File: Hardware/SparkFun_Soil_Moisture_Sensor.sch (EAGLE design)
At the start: 10 parts, among them Q1 2N3904

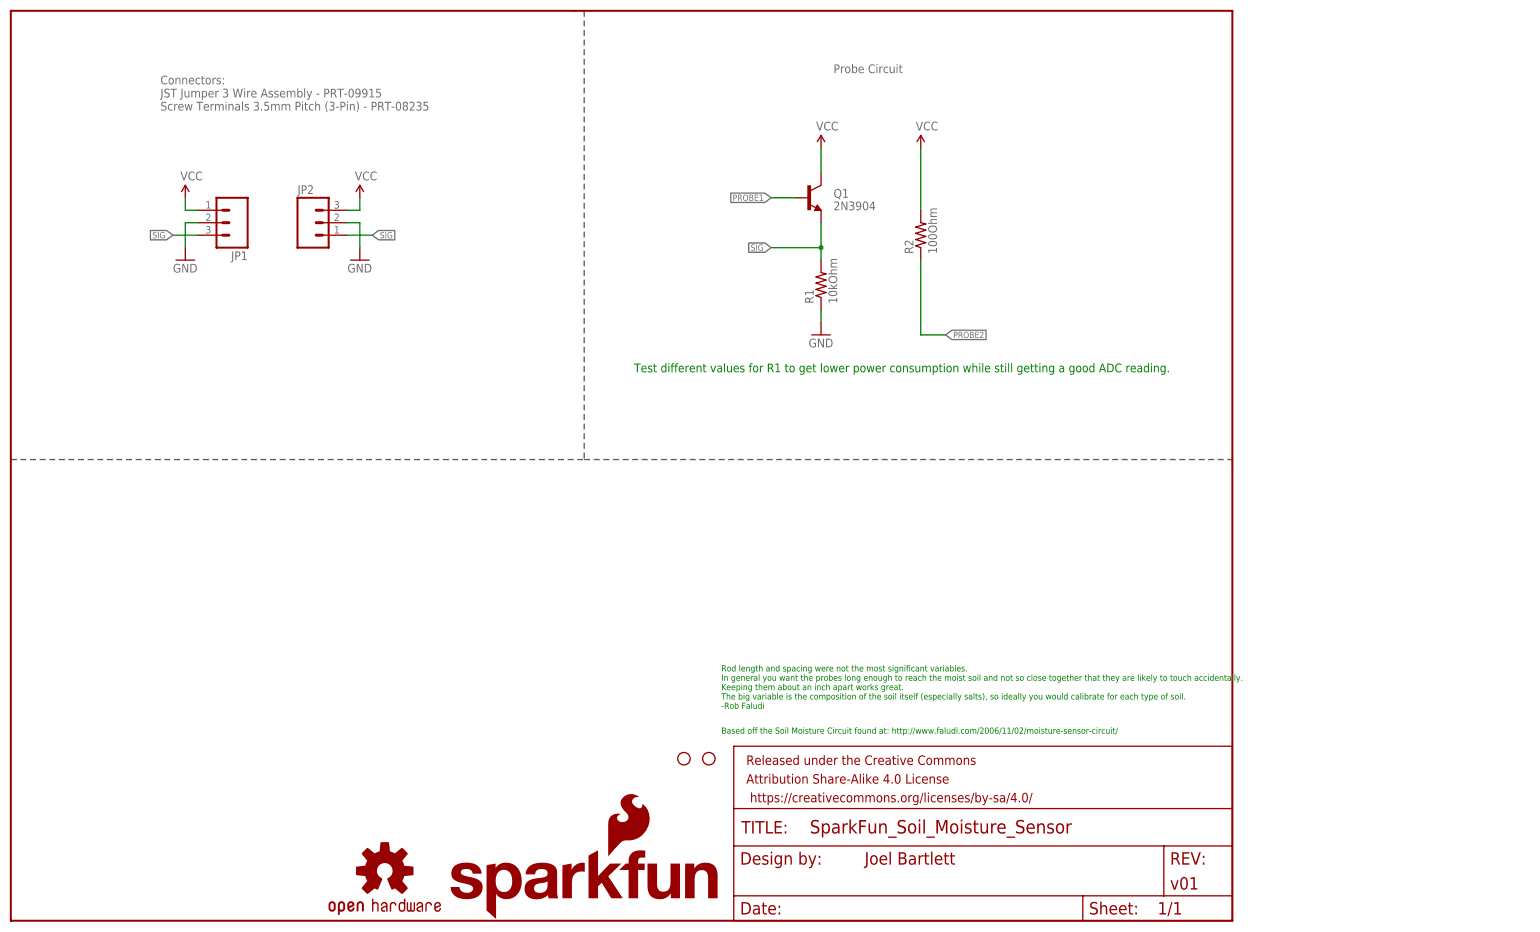
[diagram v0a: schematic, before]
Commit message: Fixed QC Checklist issues
added fiducials, changed dimension width to .008, removed Ohm from
values, added Vcc range, changed version # to correct V01, corrected
dashed lines
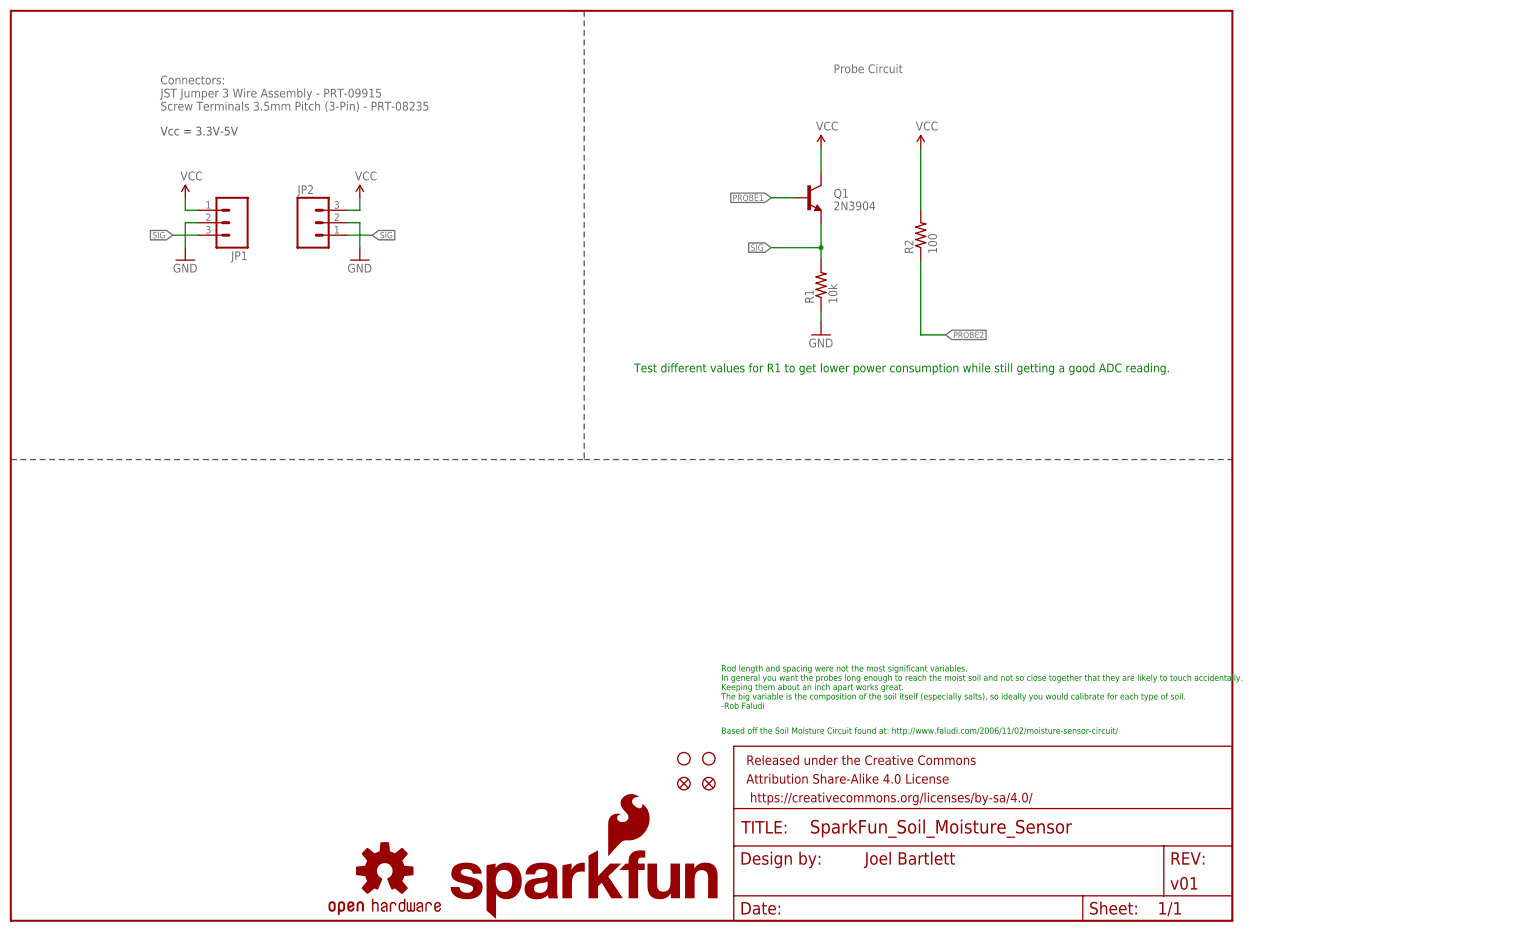
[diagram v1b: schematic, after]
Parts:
- added FID1, FID2: FIDUCIAL1X2, SparkFun-Aesthetics:FIDUCIAL1X2
- R1: value 10kOhm -> 10k
- R2: value 100Ohm -> 100
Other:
- note added: "Vcc = 3.3V-5V"
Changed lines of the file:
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@@
 <parts>
 <part name="Q1" library="SparkFun-DiscreteSemi" deviceset="TRANSISTOR_NPN" device="MMBT2222A" value="2N3904"/>
-<part name="R1" library="SparkFun-Resistors" deviceset="100OHM-1/4W-5%(0603)" device="" value="10kOhm"/>
+<part name="R1" library="SparkFun-Resistors" deviceset="100OHM-1/4W-5%(0603)" device="" value="10k"/>
 <part name="SUPPLY1" library="SparkFun-Aesthetics" deviceset="VCC" device=""/>
 <part name="GND1" library="SparkFun-Aesthetics" deviceset="GND" device=""/>
-<part name="R2" library="SparkFun-Resistors" deviceset="100OHM-1/4W-5%(0603)" device="" value="100Ohm"/>
+<part name="R2" library="SparkFun-Resistors" deviceset="100OHM-1/4W-5%(0603)" device="" value="100"/>
 <part name="SUPPLY2" library="SparkFun-Aesthetics" deviceset="VCC" device=""/>
 <part name="SUPPLY3" library="SparkFun-Aesthetics" deviceset="VCC" device=""/>
@@
 <part name="STANDOFF1" library="SparkFun-Electromechanical" deviceset="STAND-OFF" device=""/>
 <part name="STANDOFF2" library="SparkFun-Electromechanical" deviceset="STAND-OFF" device=""/>
+<part name="FID1" library="SparkFun-Aesthetics" deviceset="FIDUCIAL" device="1X2"/>
+<part name="FID2" library="SparkFun-Aesthetics" deviceset="FIDUCIAL" device="1X2"/>
 </parts>
 <sheets>
@@
 <plain>
 <text x="127" y="111.76" size="1.778" layer="91">Test different values for R1 to get lower power consumption while still getting a good ADC reading. </text>
-<wire x1="0" y1="93.98" x2="116.84" y2="93.98" width="0.2032" layer="97" style="dashdot"/>
-<wire x1="116.84" y1="93.98" x2="248.92" y2="93.98" width="0.2032" layer="97" style="dashdot"/>
+<wire x1="0" y1="93.98" x2="116.84" y2="93.98" width="0.2032" layer="97" style="shortdash"/>
+<wire x1="116.84" y1="93.98" x2="248.92" y2="93.98" width="0.2032" layer="97" style="shortdash"/>
 <wire x1="248.92" y1="93.98" x2="248.92" y2="91.44" width="0.2032" layer="97" style="dashdot"/>
 <wire x1="114.3" y1="185.42" x2="116.84" y2="185.42" width="0.2032" layer="97" style="dashdot"/>
-<wire x1="116.84" y1="185.42" x2="116.84" y2="93.98" width="0.2032" layer="97" style="dashdot"/>
+<wire x1="116.84" y1="185.42" x2="116.84" y2="93.98" width="0.2032" layer="97" style="shortdash"/>
 <text x="144.78" y="38.1" size="1.27" layer="91">Based off the Soil Moisture Circuit found at: http://www.faludi.com/2006/11/02/moisture-sensor-circuit/</text>
 <text x="144.78" y="43.18" size="1.27" layer="91">Rod length and spacing were not the most significant variables.
@@
 Screw Terminals 3.5mm Pitch (3-Pin) - PRT-08235</text>
 <text x="167.64" y="172.72" size="1.778" layer="95">Probe Circuit</text>
+<text x="30.48" y="160.02" size="1.778" layer="97">Vcc = 3.3V-5V</text>
 </plain>
 <instances>
@@
 <instance part="STANDOFF1" gate="G$1" x="137.16" y="33.02"/>
 <instance part="STANDOFF2" gate="G$1" x="142.24" y="33.02"/>
+<instance part="FID1" gate="G$1" x="137.16" y="27.94"/>
+<instance part="FID2" gate="G$1" x="142.24" y="27.94"/>
 </instances>
 <busses>

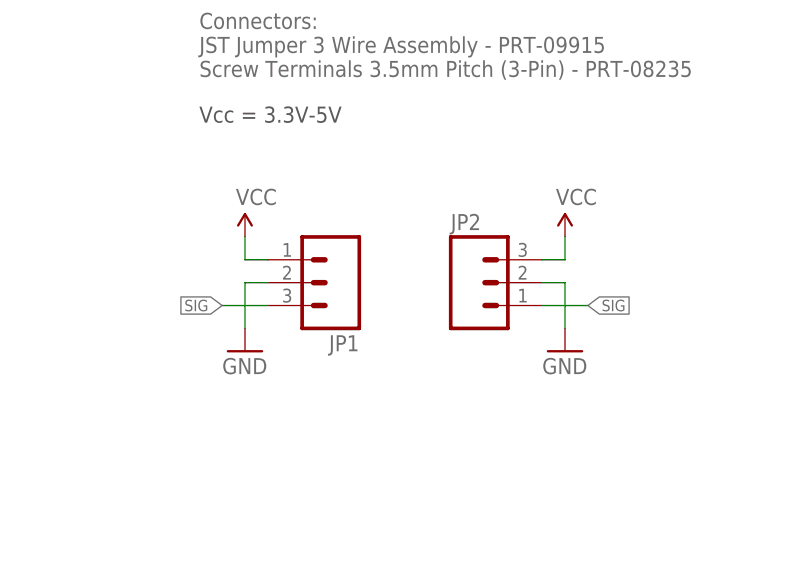
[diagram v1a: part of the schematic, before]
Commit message: Ready for QC checklist
thickened traces, few minor aesthetic changes. Updated version #.
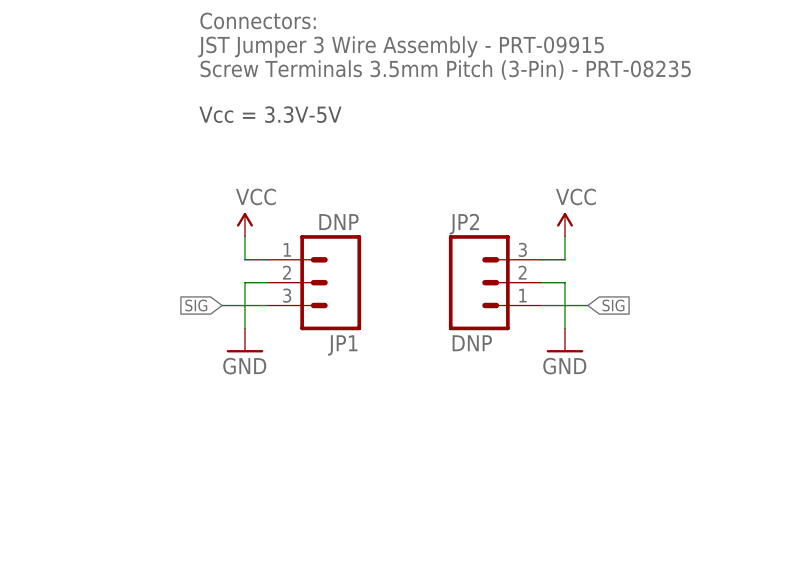
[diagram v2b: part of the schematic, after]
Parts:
- JP1, JP2: value (none) -> DNP
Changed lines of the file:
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@@
 <part name="LOGO1" library="SparkFun-Aesthetics" deviceset="SFE_LOGO_NAME_FLAME" device=".1_INCH"/>
 <part name="LOGO2" library="SparkFun-Aesthetics" deviceset="OSHW-LOGO" device="S"/>
-<part name="JP1" library="SparkFun-Connectors" deviceset="M03" device="POLAR"/>
-<part name="JP2" library="SparkFun-Connectors" deviceset="M03" device="SCREW"/>
+<part name="JP1" library="SparkFun-Connectors" deviceset="M03" device="POLAR" value="DNP"/>
+<part name="JP2" library="SparkFun-Connectors" deviceset="M03" device="SCREW" value="DNP"/>
 <part name="SUPPLY4" library="SparkFun-Aesthetics" deviceset="VCC" device=""/>
 <part name="GND3" library="SparkFun-Aesthetics" deviceset="GND" device=""/>

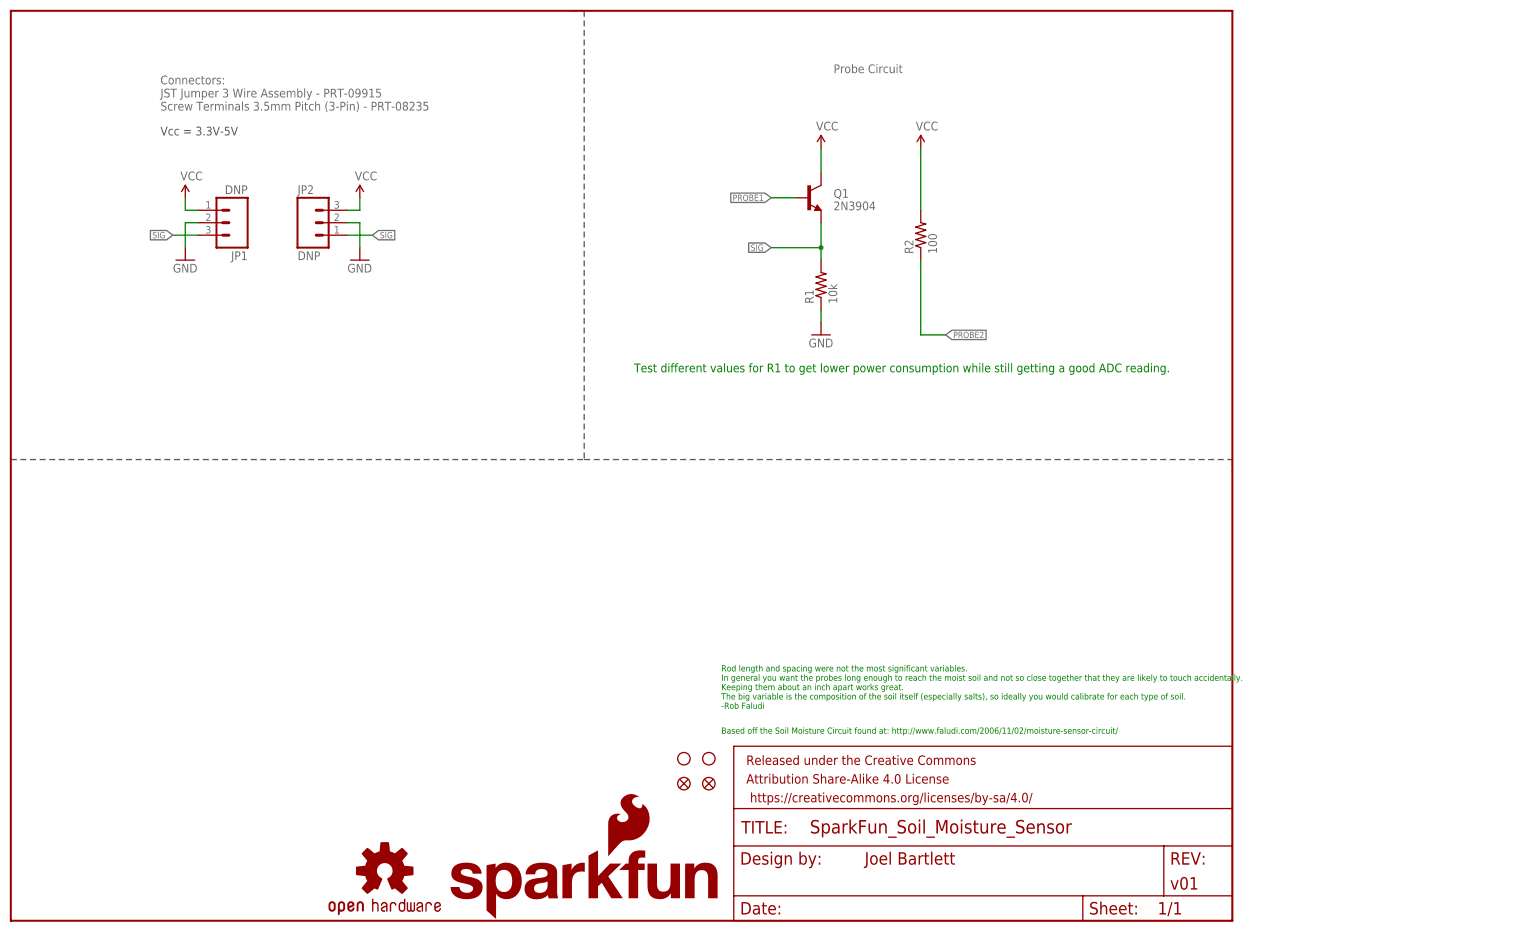
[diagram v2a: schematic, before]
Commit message: Ready for Reds
Passed QC check #2
-Comments to layer 97
-Updated Version # on SCH.
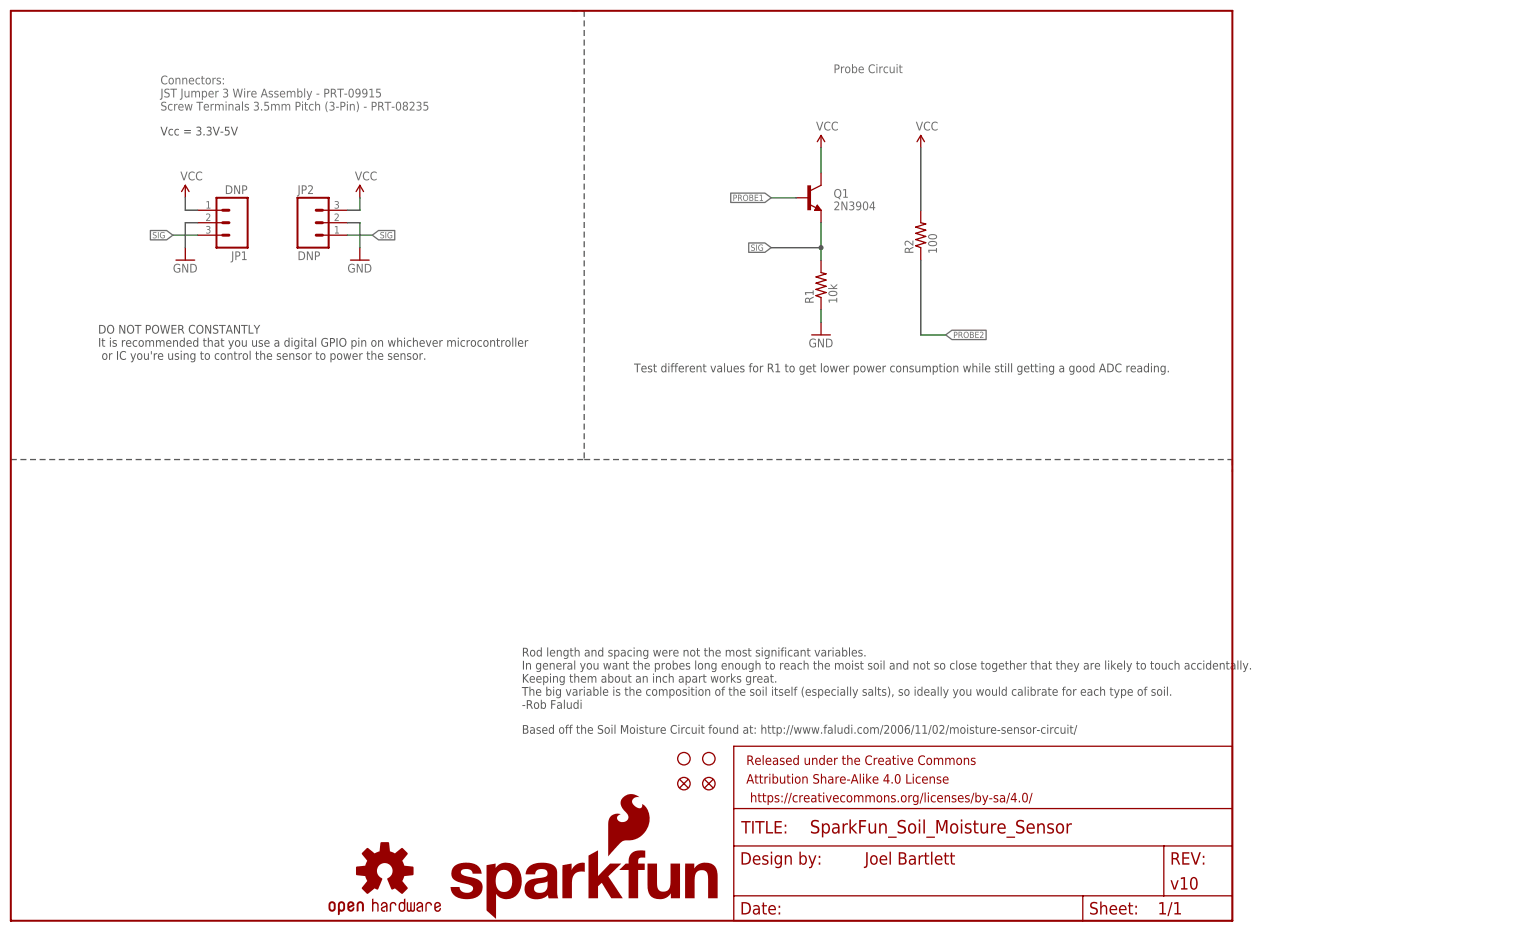
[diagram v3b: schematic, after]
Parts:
- FRAME1: VERSION (none) -> v10
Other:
- note added: "DO NOT POWER CONSTANTLY It is recommended that you use a digital GPIO pin on whichever microcontroller or IC you're using to control the sensor to power the sensor."
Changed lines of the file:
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@@
 <part name="FRAME1" library="SparkFun-Aesthetics" deviceset="FRAME-LETTER" device="">
 <attribute name="DESIGNER" value="Joel Bartlett"/>
+<attribute name="VERSION" value="v10"/>
 </part>
 <part name="LOGO1" library="SparkFun-Aesthetics" deviceset="SFE_LOGO_NAME_FLAME" device=".1_INCH"/>
@@
 <sheet>
 <plain>
-<text x="127" y="111.76" size="1.778" layer="91">Test different values for R1 to get lower power consumption while still getting a good ADC reading. </text>
+<text x="127" y="111.76" size="1.778" layer="97">Test different values for R1 to get lower power consumption while still getting a good ADC reading. </text>
 <wire x1="0" y1="93.98" x2="116.84" y2="93.98" width="0.2032" layer="97" style="shortdash"/>
 <wire x1="116.84" y1="93.98" x2="248.92" y2="93.98" width="0.2032" layer="97" style="shortdash"/>
@@
 <wire x1="114.3" y1="185.42" x2="116.84" y2="185.42" width="0.2032" layer="97" style="dashdot"/>
 <wire x1="116.84" y1="185.42" x2="116.84" y2="93.98" width="0.2032" layer="97" style="shortdash"/>
-<text x="144.78" y="38.1" size="1.27" layer="91">Based off the Soil Moisture Circuit found at: http://www.faludi.com/2006/11/02/moisture-sensor-circuit/</text>
-<text x="144.78" y="43.18" size="1.27" layer="91">Rod length and spacing were not the most significant variables.
+<text x="104.14" y="38.1" size="1.778" layer="97">Based off the Soil Moisture Circuit found at: http://www.faludi.com/2006/11/02/moisture-sensor-circuit/</text>
+<text x="104.14" y="43.18" size="1.778" layer="97">Rod length and spacing were not the most significant variables.
 In general you want the probes long enough to reach the moist soil and not so close together that they are likely to touch accidentally.
 Keeping them about an inch apart works great.
@@
 <text x="167.64" y="172.72" size="1.778" layer="95">Probe Circuit</text>
 <text x="30.48" y="160.02" size="1.778" layer="97">Vcc = 3.3V-5V</text>
+<text x="17.78" y="114.3" size="1.778" layer="97">DO NOT POWER CONSTANTLY
+It is recommended that you use a digital GPIO pin on whichever microcontroller
+ or IC you're using to control the sensor to power the sensor. </text>
 </plain>
 <instances>
